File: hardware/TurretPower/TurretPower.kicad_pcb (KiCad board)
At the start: 2 copper layers, 9 parts, among them J1 5V1_Power_In, J2 3_Way_Power_Out

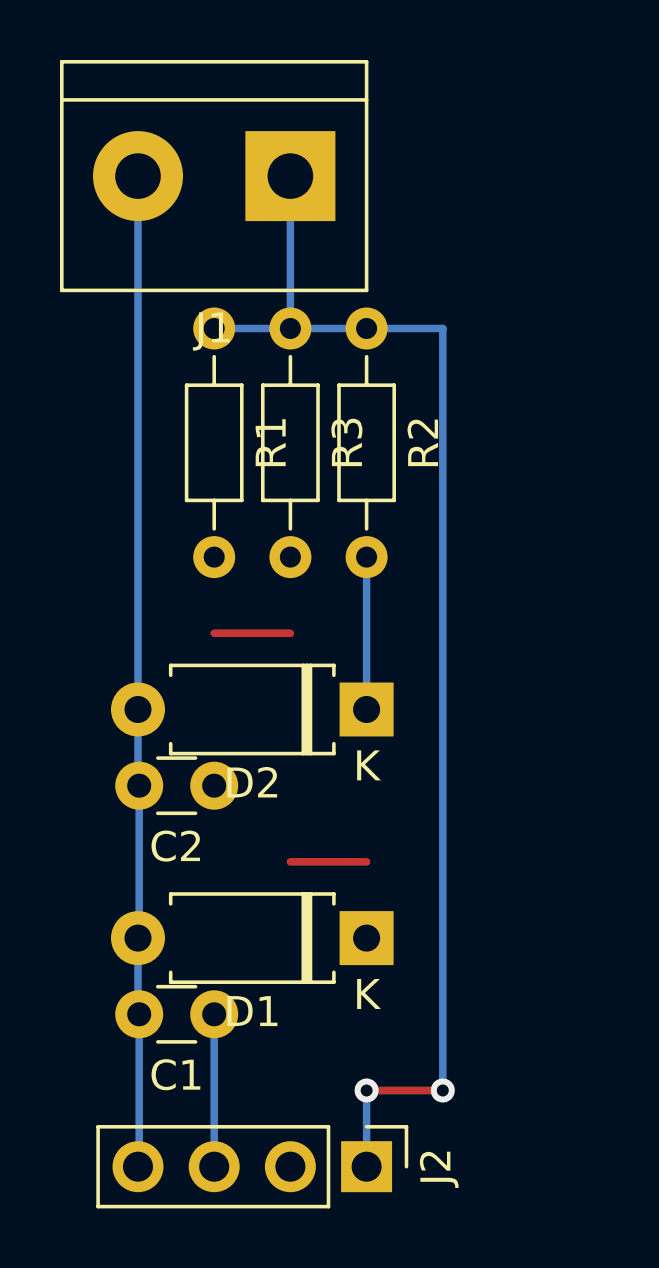
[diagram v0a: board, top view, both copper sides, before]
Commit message: Finished (and simplified) power supply board * I have built it, but I made it mirrored by mistake. No issues,   though.
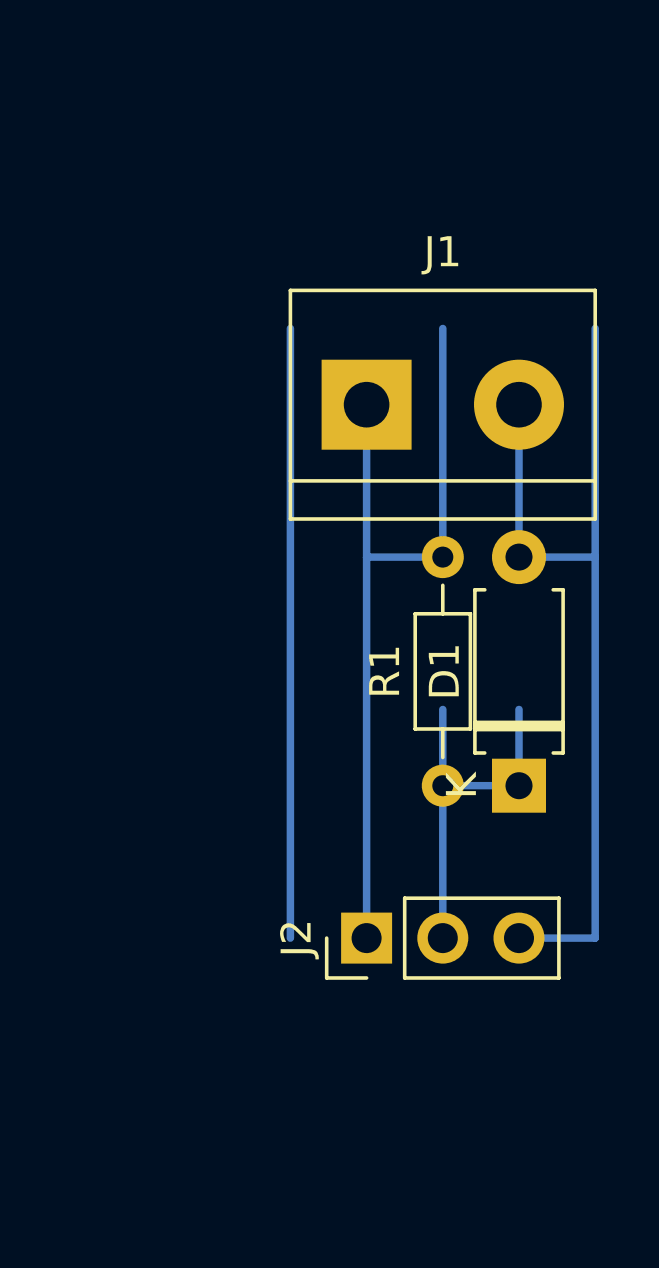
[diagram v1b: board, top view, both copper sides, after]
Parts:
- removed C1, C2: 0.1uF, Capacitor_THT:C_Disc_D3.0mm_W1.6mm_P2.50mm
- removed D2: 5V1, Diode_THT:D_A-405_P7.62mm_Horizontal
- removed R2, R3: 10, Resistor_THT:R_Axial_DIN0204_L3.6mm_D1.6mm_P7.62mm_Horizontal
- J2: footprint Connector_PinHeader_2.54mm:PinHeader_1x04_P2.54mm_Vertical -> Connector_PinHeader_2.54mm:PinHeader_1x03_P2.54mm_Vertical
- moved R1 17.0 mm to (139.7, 83.8), turned to 90 degrees
- moved J1 8.03 mm to (137.2, 71.1), turned to 0 degrees
- moved J2 7.62 mm to (137.2, 88.9), turned to 90 degrees
- moved D1 7.18 mm to (142.2, 83.8), turned to 90 degrees
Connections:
- D1 pad 1: /3V3_80mA_Regulated_Out -> /3V3_Power_Out
- J2 pad 2: /5V1_200mA_Regulated_Out -> /3V3_Power_Out
- J2 pad 3: /3V3_80mA_Regulated_Out -> /GND
- R1 pad 1: /5V1_In -> /3V3_Power_Out
- R1 pad 2: /3V3_80mA_Regulated_Out -> /5V1_In
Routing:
- net /5V1_In: track 43.2 -> 26.7 mm, vias 2 -> 0
- net (no net): track 5.08 -> 20.3 mm
- net /3V3_Power_Out: track 0.00 -> 12.7 mm
- net /5V1_200mA_Regulated_Out: track 5.08 -> 0.00 mm
- net /3V3_80mA_Regulated_Out: track 5.08 -> 0.00 mm
- net /GND: track 33.1 -> 29.2 mm
